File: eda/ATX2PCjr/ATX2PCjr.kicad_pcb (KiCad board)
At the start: 2 copper layers, 81.8 x 46.1 mm, 5 parts, among them J1 ATX Connector, J2 PCjr Card Edge, J3 Power Switch Header, J4 Fan Header, J5 Floppy Power

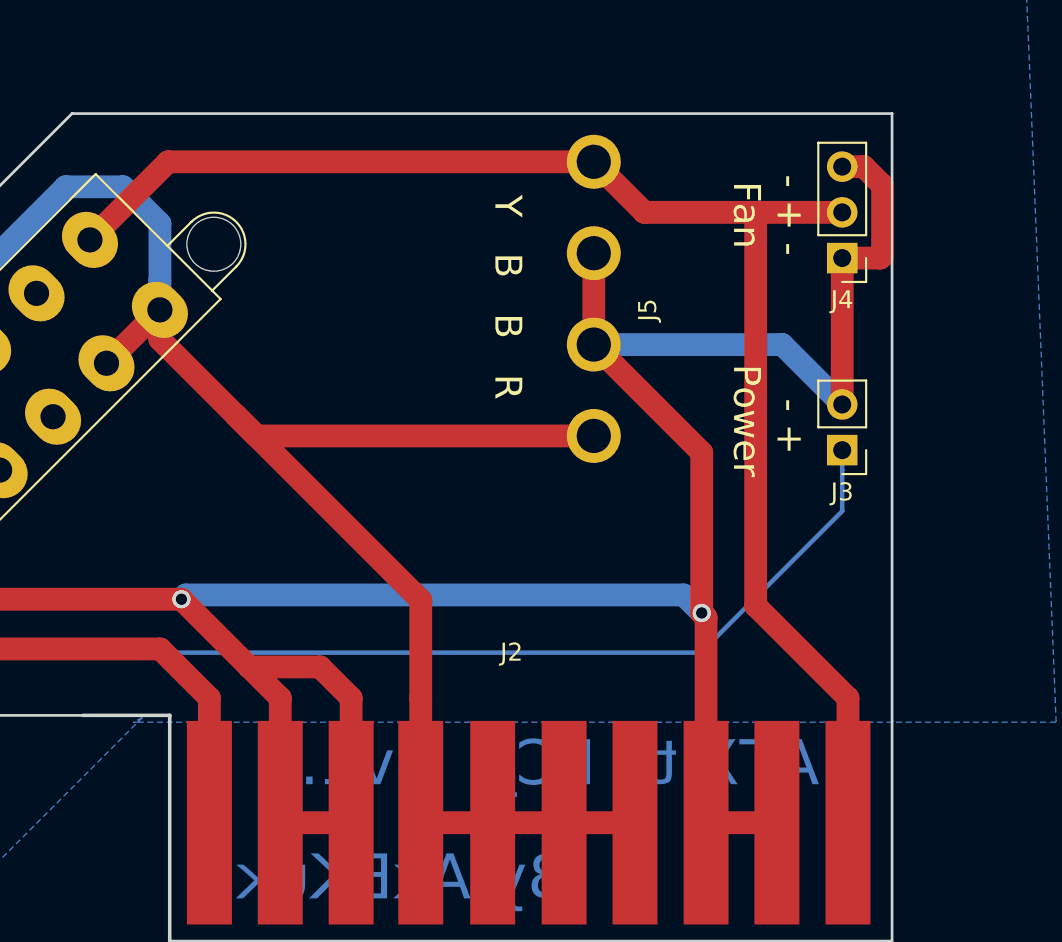
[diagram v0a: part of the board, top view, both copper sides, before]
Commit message: Updated to v1.11 to fix minor issues
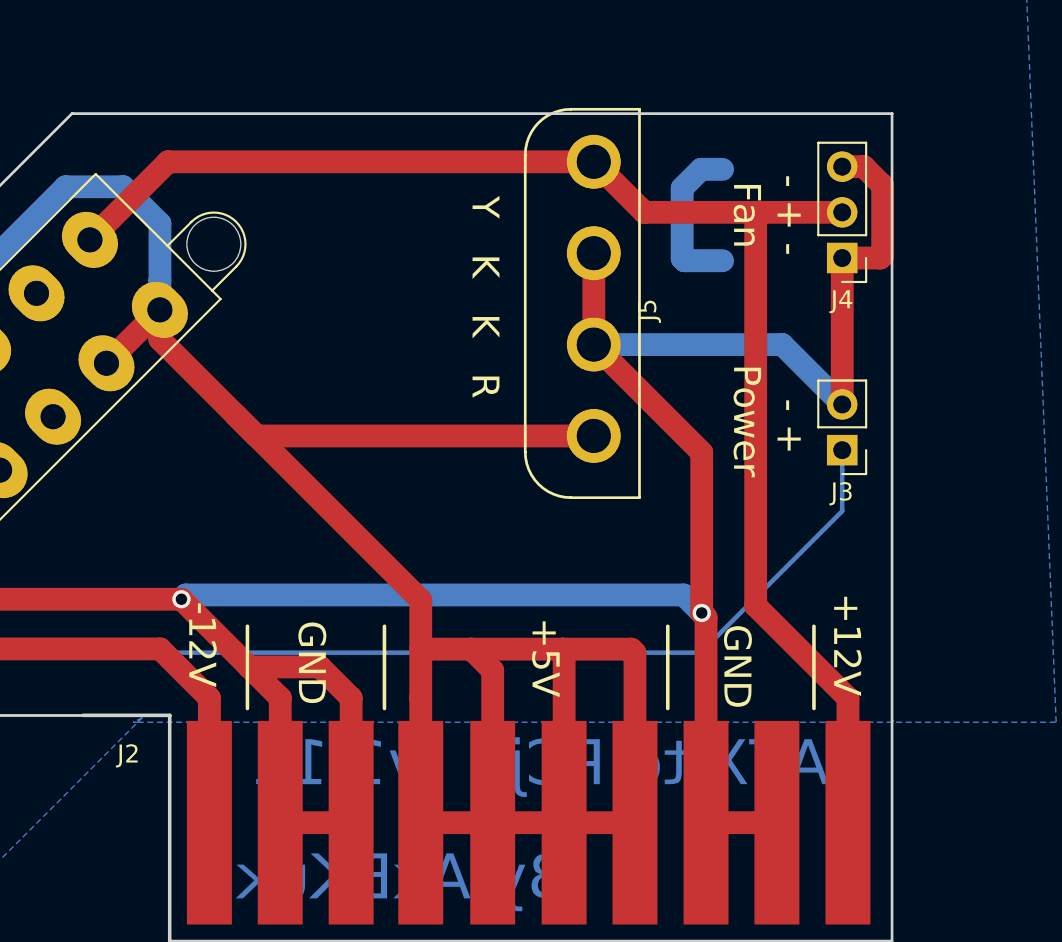
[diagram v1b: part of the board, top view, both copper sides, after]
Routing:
- net /+5V: track 112.0 -> 153.3 mm
- net /GND: track 184.2 -> 193.1 mm
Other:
- board text added: "+12V"
- board text added: "+5V"
- board text added: "-12V"
- board text added: "ATX to PCjr v1.11"
- board text added: "GND"
- board text added: "Y K K R"
- board text removed: "ATX to PCjr v1.1"
- board text removed: "Y B B R"
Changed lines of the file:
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@@
   (general
     (thickness 1.6)
-    (drawings 21)
-    (tracks 79)
+    (drawings 30)
+    (tracks 94)
     (zones 0)
     (modules 5)
@@
     (add_net /-12V)
     (add_net /GND)
+  )
+  (module "ATX2PCjr:Mate-N-Lok Vertical" (layer F.Cu)
+    (at 130 60.16 90)
+    (fp_text reference J5 (at -1 3 90) (layer F.SilkS)
+      (effects (font (size 1 1) (thickness 0.15)))
+    )
+    (fp_text value "Floppy Power" (at 0 -3 90) (layer F.Fab)
+      (effects (font (size 1 1) (thickness 0.15)))
+    )
+    (fp_line (start -11.43 2.54) (end -11.43 -1.27) (layer F.SilkS) (width 0.15))
+    (fp_line (start 10.16 2.54) (end -11.43 2.54) (layer F.SilkS) (width 0.15))
+    (fp_line (start 10.16 -1.27) (end 10.16 2.54) (layer F.SilkS) (width 0.15))
+    (fp_line (start -8.89 -3.81) (end 7.62 -3.81) (layer F.SilkS) (width 0.15))
+    (fp_arc (start 7.62 -1.27) (end 10.16 -1.27) (angle -90) (layer F.SilkS) (width 0.15))
+    (fp_arc (start -8.89 -1.27) (end -8.89 -3.81) (angle -90) (layer F.SilkS) (width 0.15))
+    (pad 4 thru_hole circle (at 7.24 0 90) (size 3 3) (drill 1.9) (layers *.Cu *.Mask)
+      (net 7 /+12V))
+    (pad 3 thru_hole circle (at 2.16 0 90) (size 3 3) (drill 1.9) (layers *.Cu *.Mask)
+      (net 3 /GND))
+    (pad 2 thru_hole circle (at -2.92 0 90) (size 3 3) (drill 1.9) (layers *.Cu *.Mask)
+      (net 3 /GND))
+    (pad 1 thru_hole circle (at -8 0 90) (size 3 3) (drill 1.9) (layers *.Cu *.Mask)
+      (net 4 /+5V))
   )
   (module Connector_Molex:Molex_Mini-Fit_Jr_5566-20A2_2x10_P4.20mm_Vertical (layer F.Cu)
@@
   (module "ATX2PCjr:PCjr Power Board Card Edge" (layer F.Cu)
     (at 106.38 84)
-    (fp_text reference J2 (at 19.05 -3.81) (layer F.SilkS)
+    (fp_text reference J2 (at -2.24 1.852) (layer F.SilkS)
       (effects (font (size 1 1) (thickness 0.15)))
     )
@@
     )
   )
-  (module "ATX2PCjr:Mate-N-Lok Vertical" (layer F.Cu)
-    (at 130 60.16 90)
-    (fp_text reference J5 (at -1 3 90) (layer F.SilkS)
-      (effects (font (size 1 1) (thickness 0.15)))
-    )
-    (fp_text value "Floppy Power" (at 0 -3 90) (layer F.Fab)
-      (effects (font (size 1 1) (thickness 0.15)))
-    )
-    (pad 1 thru_hole circle (at -8 0 90) (size 3 3) (drill 1.9) (layers *.Cu *.Mask)
-      (net 4 /+5V))
-    (pad 2 thru_hole circle (at -2.92 0 90) (size 3 3) (drill 1.9) (layers *.Cu *.Mask)
-      (net 3 /GND))
-    (pad 3 thru_hole circle (at 2.16 0 90) (size 3 3) (drill 1.9) (layers *.Cu *.Mask)
-      (net 3 /GND))
-    (pad 4 thru_hole circle (at 7.24 0 90) (size 3 3) (drill 1.9) (layers *.Cu *.Mask)
-      (net 7 /+12V))
-  )
-  (gr_text "Y   B   B   R" (at 125.222 60.452 270) (layer F.SilkS)
+  (gr_text "- + -\nFan" (at 139.7 55.88 270) (layer F.SilkS)
+    (effects (font (size 1.5 1.5) (thickness 0.3)))
+  )
+  (gr_text +12V (at 144.054 79.756 270) (layer F.SilkS)
+    (effects (font (size 1.5 1.5) (thickness 0.3)))
+  )
+  (gr_text -12V (at 108.204 79.756 270) (layer F.SilkS)
+    (effects (font (size 1.5 1.5) (thickness 0.3)))
+  )
+  (gr_text GND (at 137.958 80.978 270) (layer F.SilkS)
+    (effects (font (size 1.5 1.5) (thickness 0.3)))
+  )
+  (gr_text GND (at 114.3 80.772 270) (layer F.SilkS)
+    (effects (font (size 1.5 1.5) (thickness 0.3)))
+  )
+  (gr_line (start 110.744 83.312) (end 110.744 78.74) (layer F.SilkS) (width 0.2))
+  (gr_line (start 118.364 83.312) (end 118.364 78.74) (layer F.SilkS) (width 0.2))
+  (gr_line (start 142.24 83.312) (end 142.24 78.74) (layer F.SilkS) (width 0.2))
+  (gr_line (start 134.112 83.312) (end 134.112 78.74) (layer F.SilkS) (width 0.2))
+  (gr_text +5V (at 127.29 80.47 270) (layer F.SilkS)
+    (effects (font (size 1.5 1.5) (thickness 0.3)))
+  )
+  (gr_text "Y   K   K   R" (at 123.952 60.452 270) (layer F.SilkS)
     (effects (font (size 1.5 1.5) (thickness 0.3)))
   )
@@
     (effects (font (size 1.5 1.5) (thickness 0.3)))
   )
-  (gr_text "- + -\nFan" (at 139.7 55.88 270) (layer F.SilkS)
-    (effects (font (size 1.5 1.5) (thickness 0.3)))
-  )
   (gr_text "By AkBKukU" (at 118.11 92.71) (layer B.Cu)
     (effects (font (size 2.5 2.5) (thickness 0.3)) (justify mirror))
   )
-  (gr_text "ATX to PCjr    v1.1" (at 127 86.36) (layer B.Cu)
+  (gr_text "ATX to PCjr   v1.11" (at 127 86.36) (layer B.Cu)
     (effects (font (size 2.5 2.5) (thickness 0.3)) (justify mirror))
   )
@@
   (segment (start 140.48 63.08) (end 130 63.08) (width 1.27) (layer B.Cu) (net 3))
   (segment (start 143.81 66.41) (end 140.48 63.08) (width 1.27) (layer B.Cu) (net 3))
+  (segment (start 134.912999 54.38492) (end 134.912999 58.292999) (width 1.27) (layer B.Cu) (net 3))
+  (segment (start 135.957919 53.34) (end 134.912999 54.38492) (width 1.27) (layer B.Cu) (net 3))
+  (segment (start 135.04 58.42) (end 137.16 58.42) (width 1.27) (layer B.Cu) (net 3))
+  (segment (start 134.912999 58.292999) (end 135.04 58.42) (width 1.27) (layer B.Cu) (net 3))
+  (segment (start 137.16 53.34) (end 135.957919 53.34) (width 1.27) (layer B.Cu) (net 3))
   (segment (start 102.909546 64.120606) (end 105.879394 61.150758) (width 1.27) (layer F.Cu) (net 4))
   (segment (start 102.909545 64.120606) (end 102.909546 64.120606) (width 1.27) (layer F.Cu) (net 4))
   (segment (start 120.38 82.73) (end 120.38 89.66) (width 1.27) (layer F.Cu) (net 4))
-  (segment (start 120.38 77.291701) (end 120.38 82.73) (width 1.27) (layer F.Cu) (net 4))
   (segment (start 105.879394 61.150758) (end 105.879394 62.791095) (width 1.27) (layer F.Cu) (net 4))
   (segment (start 120.38 89.66) (end 124.38 89.66) (width 1.27) (layer F.Cu) (net 4))
@@
   (segment (start 90.110912 64.831941) (end 100.635187 54.307666) (width 1.27) (layer B.Cu) (net 4))
   (segment (start 90.110912 69.141065) (end 90.110912 64.831941) (width 1.27) (layer B.Cu) (net 4))
+  (segment (start 120.38 80.01) (end 123.19 80.01) (width 1.27) (layer F.Cu) (net 4))
+  (segment (start 120.38 80.01) (end 120.38 82.73) (width 1.27) (layer F.Cu) (net 4))
+  (segment (start 120.38 77.291701) (end 120.38 80.01) (width 1.27) (layer F.Cu) (net 4))
+  (segment (start 124.38 81.2) (end 124.38 89.66) (width 1.27) (layer F.Cu) (net 4))
+  (segment (start 123.19 80.01) (end 124.38 81.2) (width 1.27) (layer F.Cu) (net 4))
+  (segment (start 123.19 80.01) (end 128.27 80.01) (width 1.27) (layer F.Cu) (net 4))
+  (segment (start 128.35 80.09) (end 128.35 89.66) (width 1.27) (layer F.Cu) (net 4))
+  (segment (start 128.27 80.01) (end 128.35 80.09) (width 1.27) (layer F.Cu) (net 4))
+  (segment (start 128.27 80.01) (end 132.08 80.01) (width 1.27) (layer F.Cu) (net 4))
+  (segment (start 132.29 80.22) (end 132.29 89.66) (width 1.27) (layer F.Cu) (net 4))
+  (segment (start 132.08 80.01) (end 132.29 80.22) (width 1.27) (layer F.Cu) (net 4))
   (segment (start 106.331977 52.92) (end 130 52.92) (width 1.27) (layer F.Cu) (net 7))
   (segment (start 101.990306 57.261671) (end 106.331977 52.92) (width 1.27) (layer F.Cu) (net 7))

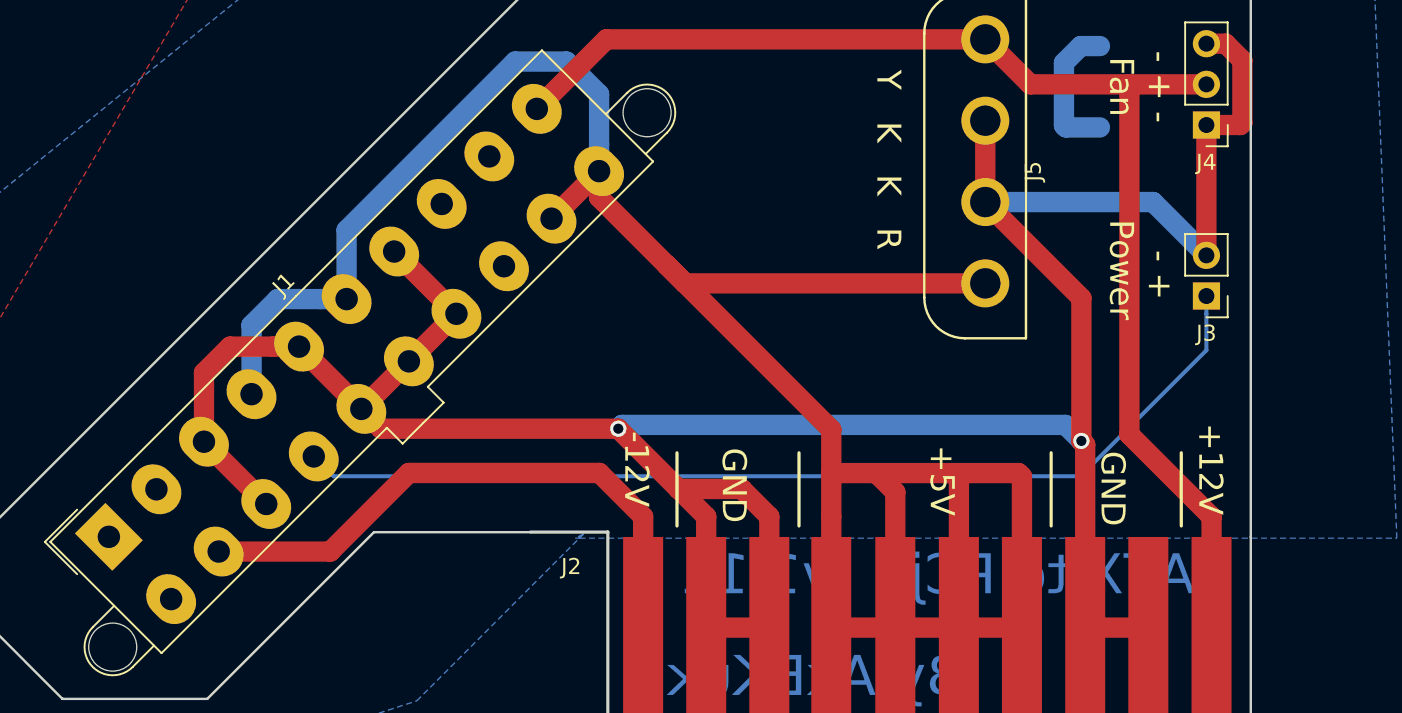
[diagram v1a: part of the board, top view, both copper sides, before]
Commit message: MiniFit Jr Vias and Panel Holes
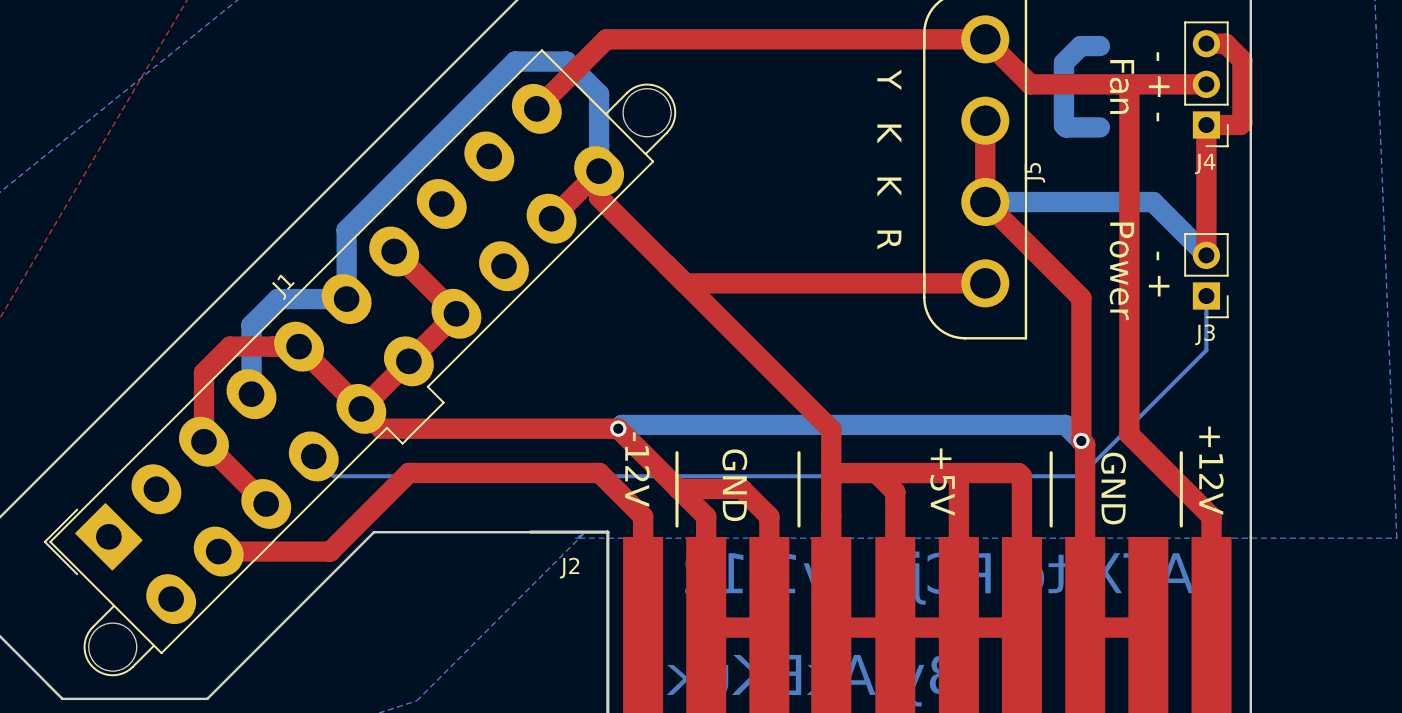
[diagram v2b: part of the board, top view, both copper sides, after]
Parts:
- J1: footprint Connector_Molex:Molex_Mini-Fit_Jr_5566-20A2_2x10_P4.20mm_Vertical -> ATX2PCjr:Molex_Mini-Fit_Jr_5566-20A2_2x10_P4.20mm_Vertical-LARGE
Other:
- board text added: "ATX to PCjr v1.12"
- board text removed: "ATX to PCjr v1.11"
